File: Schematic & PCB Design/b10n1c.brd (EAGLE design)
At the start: 14 x 44 mm, 63 parts, among them U1 nRF8001, U2 ATMEGA328P-MU, U3 PN532, Y1 16MHz, Y2 32.768, Y3 8MHZ, Y4 27.12MHz

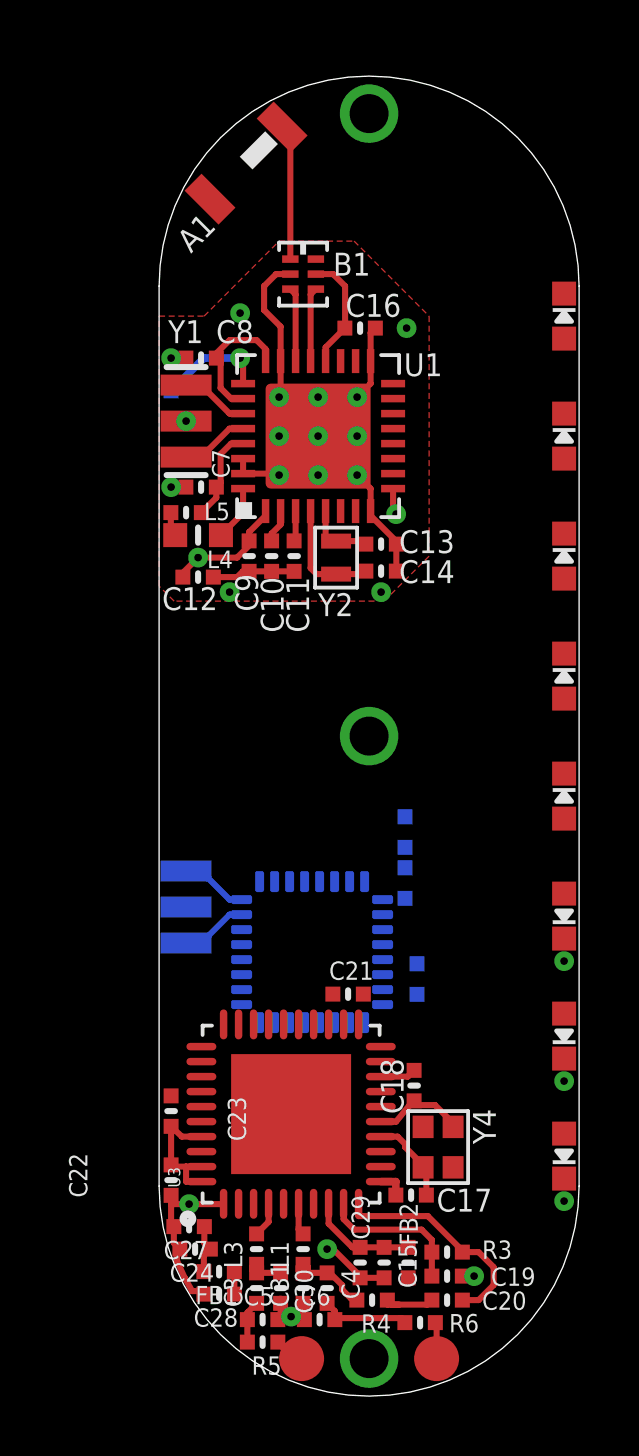
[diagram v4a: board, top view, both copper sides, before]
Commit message: PN532 PCB layout completed
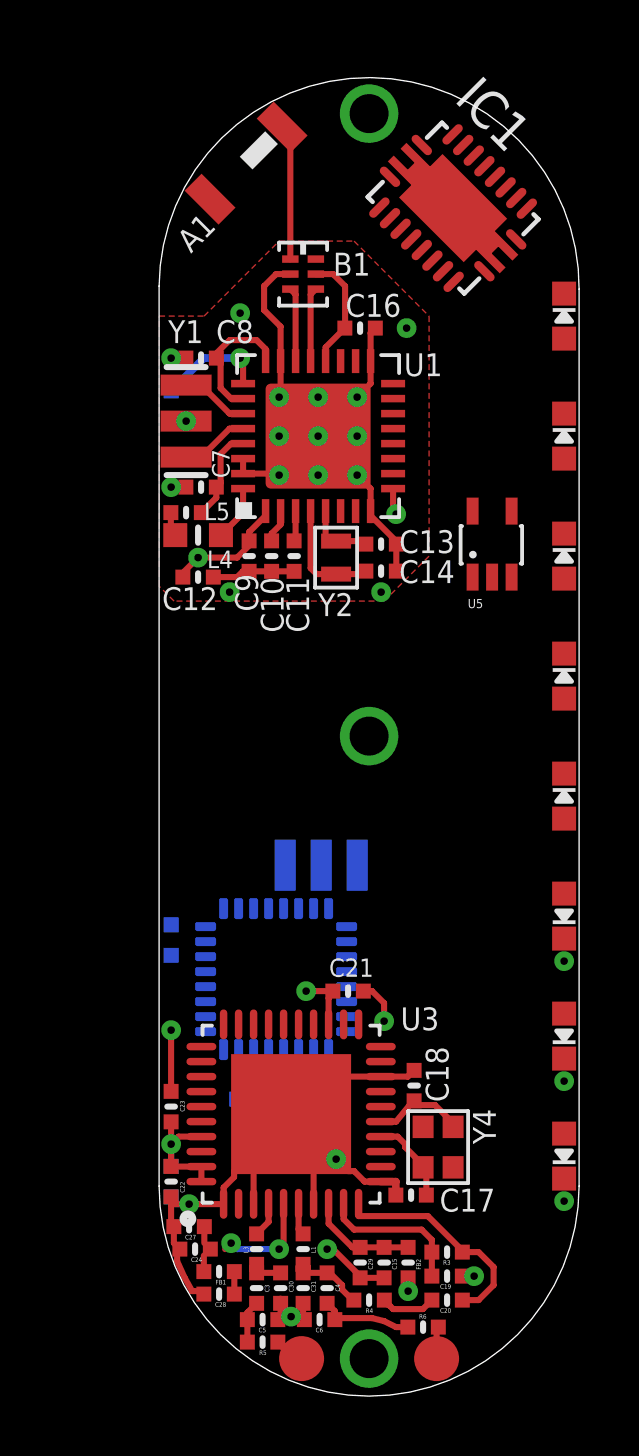
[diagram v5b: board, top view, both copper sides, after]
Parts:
- added C25: 10µF, microbuilder:_0402MP
- added IC1: BQ51013A, bq500211_bq500210_bq51013a:RHL_R-VQFN-N20
- added U5: TLV700XX, WirelessPower:SC70-5
- C13, C14: value 9pF -> 8pF
- C17, C18: value 33pF -> 8pF
- moved C1 9.42 mm to (5.10, 2.90), turned to 0 degrees
- moved C2 8.82 mm to (3.10, 2.90), turned to 180 degrees
- moved R2 8.30 mm to (0.40, 8.20)
- moved Y3 4.71 mm to (5.40, 10.7), turned to 0 degrees
- moved U2 1.50 mm to (3.90, 6.90), turned to 270 degrees
- moved R6 0.18 mm to (8.80, -4.70)
- moved C23 0.15 mm to (0.40, 2.65)
- moved C21 0.10 mm to (6.30, 6.50)
- moved R4 0.10 mm to (7.00, -3.80)
- moved C22 0.05 mm to (0.40, 0.15)
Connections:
- removed net +3V3: C1.1, R2.2, U2.18, U2.4, U2.6
- removed net IO4: LED3.A, U2.2
- new net IN: U5.1
- new net IO10: LED3.A, U2.14
- new net OUT: U5.5
- net ADC6: now also LED2.A
- net ADC7: now also LED1.A
- net GND: now also C25.2, U5.2
- net IO2: no longer LED1.A
- net IO3: no longer LED2.A
- net IO5: now also LED8.A; no longer LED4.A
- net IO6: now also LED7.A; no longer LED5.A
- net IO8: now also LED5.A; no longer LED7.A
- net IO9: now also LED4.A; no longer LED8.A
- net IRQ: now also U2.2
- net REQ: no longer U2.14
- net VDD: now also C1.1, C25.1, R2.2, U2.18, U2.4, U2.6
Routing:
- net GND: track 13.5 -> 36.0 mm, vias 7 -> 10
- net N$30: track 1.67 -> 4.62 mm, vias 0 -> 2
- net VDD: track 5.23 -> 8.08 mm, vias 0 -> 3
- net N$4: track 2.24 -> 0.00 mm
- net N$6: track 2.24 -> 0.00 mm
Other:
- outline, holes or cut-outs redrawn

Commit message: bq51013A schematic added
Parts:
- added C26, C32, C33, C34, C35, C36, C37, C38, C39, C40, C41, C42, C43, C44, C45, C46, C47, C48: 0.1µF, microbuilder:_0402MP
- added R10, R7, R8, R9: 10K, microbuilder:_0402MP
- added TP3, TP4: AC1, microbuilder:TESTPOINT_ROUND_1MM
- moved IC1 0.10 mm to (9.90, 32.6), turned to 270 degrees
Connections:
- new net AC1: C32.2, C33.2, C34.2, C44.1, C45.1, TP3.P$1
- new net AC2: C38.1, C39.1, C40.1, C44.2, C45.2, IC1.19, TP4.P$1
- new net COIL_CHRG_OUT: C46.1, C47.1, C48.1, IC1.4, R10.2
- new net N$31: C32.1, C33.1, C34.1, C35.2, C36.2, C37.2, IC1.2
- new net N$33: C40.2, IC1.17
- new net N$34: C41.2, C42.2, C43.2, IC1.18
- new net N$35: C37.1, IC1.3
- new net N$36: C36.1, IC1.5
- new net N$37: C35.1, IC1.6
- new net N$38: C39.2, IC1.16
- new net N$39: C38.2, IC1.15
- new net N$40: IC1.14, R7.1, R9.2
- new net N$41: IC1.13, R8.2
- new net N$42: IC1.11, R10.1
- new net N$43: IC1.12, R7.2
- net GND: now also C41.1, C42.1, C43.1, C46.2, C47.2, C48.2, IC1.1, IC1.10, IC1.20, IC1.9, IC1.EXP@1, IC1.EXP@2, IC1.EXP@3, IC1.EXP@4, IC1.EXP@5, IC1.EXP@6, IC1.EXP@7, R8.1, R9.1

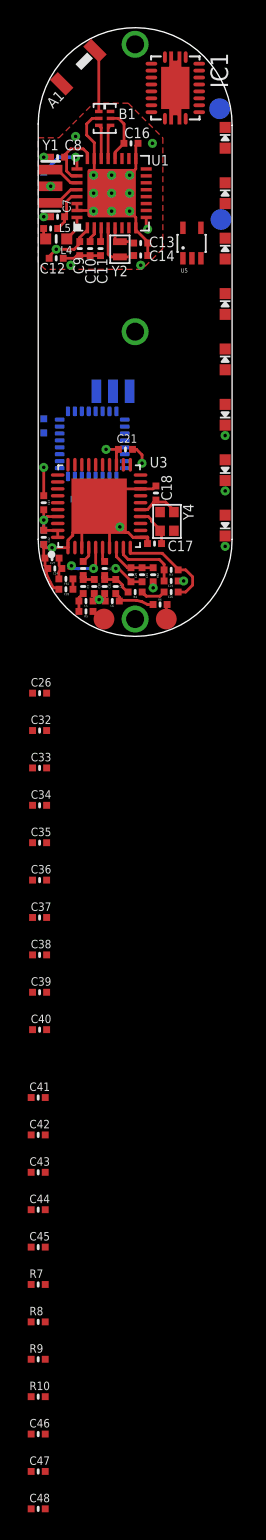
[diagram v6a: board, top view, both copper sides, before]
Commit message: Power DONE!
BQ51013 + LTC4065 + MCP1700 schematic and PCB layout DONE
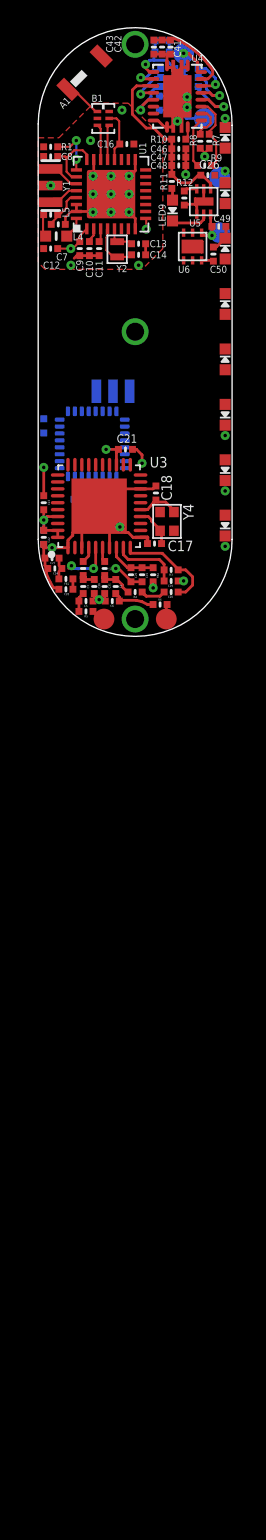
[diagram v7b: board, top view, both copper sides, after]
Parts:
- removed IC1: BQ51013A, bq500211_bq500210_bq51013a:RHL_R-VQFN-N20
- added C49, C50: 1µF, microbuilder:_0402MP
- added LED9: (no value), microbuilder:CHIPLED_0603_NOOUTLINE
- added R11: 420, microbuilder:_0402MP
- added R12: 8K, microbuilder:_0402MP
- added TP5, TP6: (no value), microbuilder:TESTPOINT_ROUND_1MM
- added U4: BQ51013A, bq500211_bq500210_bq51013a:RHL_R-VQFN-N20
- added U6: MCP1700, MCP1700:MCP1700
- C26: value 0.1µF -> 1µF
- C32, C33: value 0.1µF -> 68nF
- C34: value 0.1µF -> 47nF
- C35, C38: value 0.1µF -> 22nF
- C36, C39: value 0.1µF -> 0.47µF
- C37, C40: value 0.1µF -> 0.01µF
- C44: value 0.1µF -> 1800pF
- C45: value 0.1µF -> 100pF
- C46: value 0.1µF -> 0.1uF
- C47: value 0.1µF -> 10uF
- C48: value 0.1µF -> 10µF
- R7: value 10K -> 62
- R9: value 10K -> 200
- TP3, TP4: value AC1 -> (none)
- U5: value TLV700XX -> LTC4065L; device WirelessPower:SC70-5 -> LTC4065L:LTC4065L
- moved C48 97.5 mm to (10.2, 27.0)
- moved C47 95.4 mm to (10.2, 27.6)
- moved C46 93.4 mm to (10.2, 28.2)
- moved R10 91.4 mm to (10.2, 28.9), turned to 180 degrees
- moved R9 88.8 mm to (12.3, 28.8), turned to 90 degrees
- moved C45 86.8 mm to (8.95, 35.2), flipped to the bottom, turned to 180 degrees
- moved R8 86.0 mm to (11.7, 28.8), turned to 90 degrees
- moved C44 84.9 mm to (8.95, 36.0), flipped to the bottom, turned to 180 degrees
- moved R7 81.7 mm to (12.0, 27.0), turned to 180 degrees
- moved C43 81.7 mm to (8.35, 35.5), turned to 90 degrees
- moved C42 79.1 mm to (8.95, 35.5), turned to 90 degrees
- moved C41 76.4 mm to (9.55, 35.5), turned to 90 degrees
- moved C40 70.3 mm to (11.1, 34.0), flipped to the bottom, turned to 180 degrees
- moved C39 67.0 mm to (11.1, 33.4), flipped to the bottom, turned to 180 degrees
- moved C38 63.6 mm to (11.1, 32.7), flipped to the bottom, turned to 180 degrees
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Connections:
- net GND2 renamed AC
- removed net COIL_CHRG_OUT: C46.1, C47.1, C48.1, IC1.4, R10.2
- removed net IN: U5.1
- removed net OUT: U5.5
- new net COIL_CHRG: C26.1, C46.1, C47.1, C48.1, R10.2, R11.1, U4.4, U5.4
- new net N$32: LED9.A, R11.2
- new net N$44: LED9.C, U5.2
- new net N$45: R12.1, U5.6
- new net N$47: C49.1, TP5.P$1, U5.3, U6.1
- net AC1: no longer C44.1, C45.1
- net AC2: now also U4.19; no longer IC1.19
- net GND: now also C26.2, C49.2, C50.2, R12.2, TP6.P$1, U4.1, U4.10, U4.20, U4.9, U4.EXP@1, U4.EXP@2, U4.EXP@3, U4.EXP@4, U4.EXP@5, U4.EXP@6, U4.EXP@7, U5.1, U5.5, U5.7, U5.71, U5.72, U6.3, U6.7, U6.71, U6.72; no longer IC1.1, IC1.10, IC1.20, IC1.9, IC1.EXP@1, IC1.EXP@2, IC1.EXP@3, IC1.EXP@4, IC1.EXP@5, IC1.EXP@6, IC1.EXP@7, U5.2
- net N$31: now also C44.1, C45.1, U4.2; no longer IC1.2
- net N$33: now also U4.17; no longer IC1.17
- net N$34: now also U4.18; no longer IC1.18
- net N$35: now also U4.3; no longer IC1.3
- net N$36: now also U4.5; no longer IC1.5
- net N$37: now also U4.6; no longer IC1.6
- net N$38: now also U4.16; no longer IC1.16
- net N$39: now also U4.15; no longer IC1.15
- net N$40: now also U4.14; no longer IC1.14
- net N$41: now also U4.13; no longer IC1.13
- net N$42: now also U4.11; no longer IC1.11
- net N$43: now also U4.12; no longer IC1.12
- net VDD: now also C50.1, U6.6
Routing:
- net GND: track 36.0 -> 57.4 mm, vias 10 -> 17
- net COIL_CHRG: track 0.00 -> 14.2 mm
- net AC: track 25.3 -> 16.9 mm, vias 16 -> 14
- net N$31: track 0.00 -> 8.22 mm, vias 0 -> 1
- net AC2: track 0.00 -> 6.57 mm, vias 0 -> 1
- net N$34: track 0.00 -> 6.40 mm
- net N$40: track 0.00 -> 5.64 mm
- net N$39: track 0.00 -> 4.58 mm, vias 0 -> 1
- net N$37: track 0.00 -> 3.91 mm, vias 0 -> 1
- net N$38: track 0.00 -> 3.85 mm, vias 0 -> 1
- net N$43: track 0.00 -> 3.63 mm
- net AC1: track 0.00 -> 3.50 mm
- net N$47: track 0.00 -> 3.21 mm, vias 0 -> 1
- net N$33: track 0.00 -> 3.05 mm, vias 0 -> 1
- net N$36: track 0.00 -> 2.99 mm, vias 0 -> 1
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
